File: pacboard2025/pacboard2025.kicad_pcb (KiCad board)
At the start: 4 copper layers, 28 parts, among them J1 XT30 Male Connector, U2 D24V50F5, U3 ProS3, U6 BNO085

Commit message: some changes to pcb
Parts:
- Conn_01x04_Socket1: footprint board1_footprints:Stemma QT -> Connector_JST:JST_SH_SM04B-SRSS-TB_1x04-1MP_P1.00mm_Horizontal
- moved Conn_01x04_Socket1 51.5 mm to (167.6, 93.3), turned to 90 degrees
- moved MOTOR2 25.4 mm to (165.4, 132.8)
- moved MC2 12.6 mm to (150.4, 141.9)
- moved XSHUT_CONN1 12.4 mm to (114.6, 132.6)
- moved C1 12.4 mm to (109.8, 113.4)
- moved C2 12.4 mm to (104.1, 113.4)
- moved C3 12.4 mm to (98.2, 113.4)
- moved LED1 12.4 mm to (110.0, 108.8)
- moved LED3 12.4 mm to (98.2, 108.7)
- moved R2 12.4 mm to (114.4, 108.6)
- moved U6 12.4 mm to (99.0, 115.9)
- moved C4 12.4 mm to (92.1, 113.5)
- moved LED2 12.4 mm to (104.1, 108.8)
- moved LED4 12.4 mm to (92.2, 108.7)
- moved J1 10.4 mm to (152.3, 112.5)
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
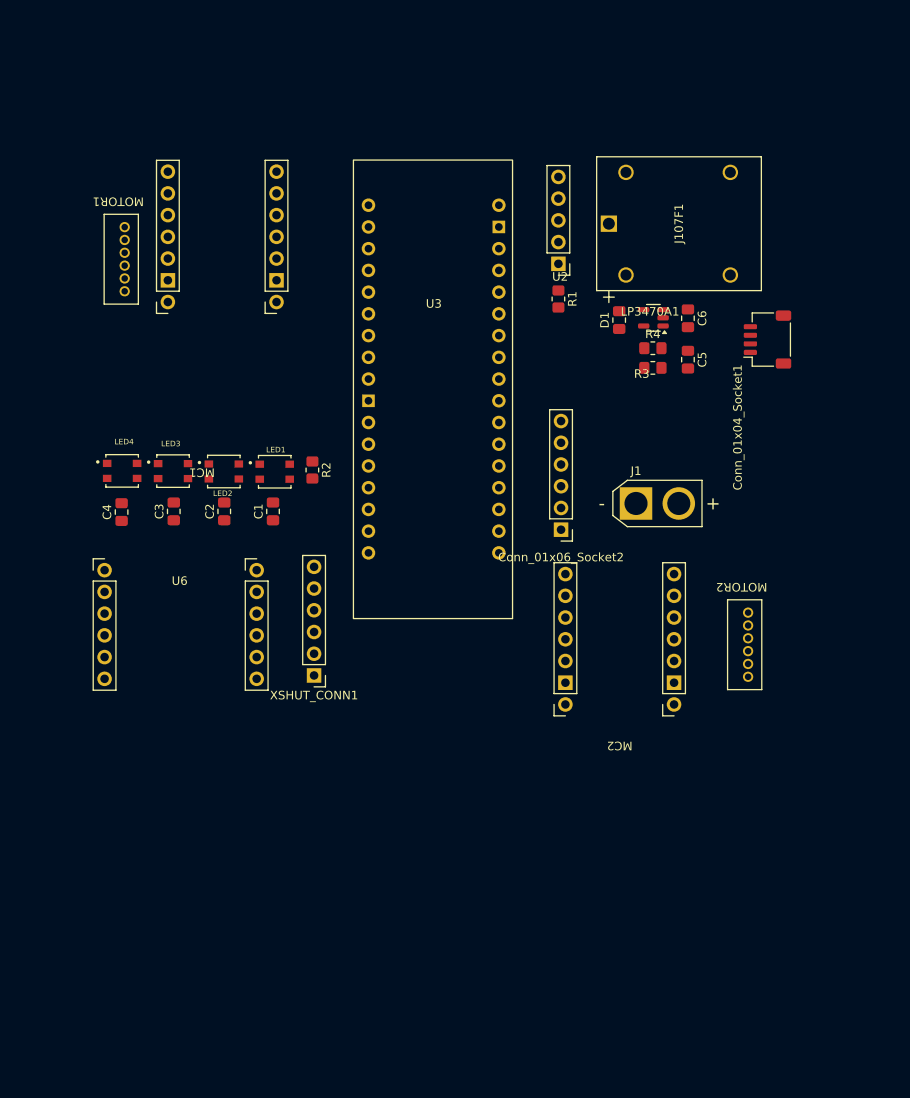
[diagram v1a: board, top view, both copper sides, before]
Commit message: Changed layout to account for battery and motors, tried routing stuff
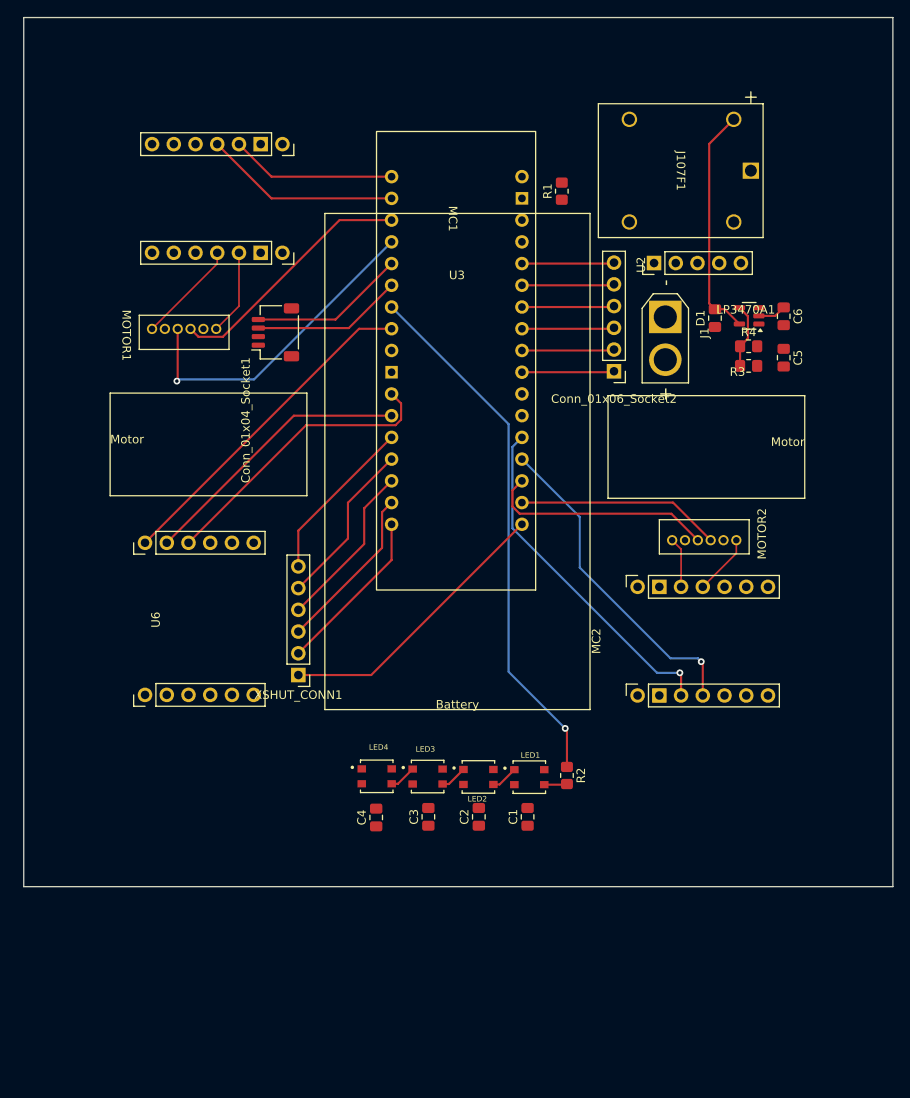
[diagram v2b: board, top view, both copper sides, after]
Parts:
- moved Conn_01x04_Socket1 57.5 mm to (110.1, 92.5)
- moved C4 46.5 mm to (121.9, 149.2)
- moved LED4 46.5 mm to (122.0, 144.4)
- moved LED1 46.5 mm to (139.8, 144.5)
- moved LED3 46.5 mm to (127.9, 144.4)
- moved R2 46.5 mm to (144.2, 144.3)
- moved C2 46.5 mm to (133.9, 149.1)
- moved C3 46.5 mm to (128.0, 149.1)
- moved LED2 46.5 mm to (133.8, 144.5)
- moved C1 46.5 mm to (139.6, 149.1)
- moved MC1 22.1 mm to (116.8, 76.8), turned to -90 degrees
- moved J1 22.1 mm to (155.7, 90.7), turned to -90 degrees
- moved Conn_01x06_Socket2 19.5 mm to (149.7, 97.0)
- moved MOTOR2 18.3 mm to (156.5, 116.8), turned to 90 degrees
- moved J107F1 17.7 mm to (165.7, 73.6), turned to -90 degrees
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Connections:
- U3 pad 13: /1_ENCA -> /2_PWM1
- U3 pad 14: /1_ENCB -> /2_PWM2
- U3 pad 31: /2_PWM2 -> /1_ENCB
- U3 pad 32: /2_PWM1 -> /1_ENCA
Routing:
- net /+12V: track 0.00 -> 132.6 mm
- net /5V: track 0.00 -> 129.8 mm
- net /BAT_12V: track 0.00 -> 63.1 mm
- net /LED_DATA: track 0.00 -> 62.3 mm, vias 0 -> 1
- net /2_PWM1: track 0.00 -> 40.4 mm, vias 0 -> 1
- net /IMU_INTR: track 0.00 -> 39.2 mm
- net /2_PWM2: track 0.00 -> 38.3 mm, vias 0 -> 1
- net /1_ENCB: track 0.00 -> 38.0 mm, vias 0 -> 1
- net /UART_TX: track 0.00 -> 34.3 mm
- net /XSHUT_TOF6: track 0.00 -> 33.4 mm
- net /UART_RX: track 0.00 -> 32.4 mm
- net /1_ENCA: track 0.00 -> 29.5 mm
- net Net-(D1-A): track 0.00 -> 27.2 mm
- net /2_ENCA: track 0.00 -> 26.8 mm
- net /2_ENCB: track 0.00 -> 23.9 mm
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- added copper zone on In2.Cu, net /+3.3V
- added copper zone on In1.Cu, net /GND
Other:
- board outline added: 101.6 x 101.6 mm
- board text added: "Battery"
- board text added: "Motor"

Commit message: new chassis shape
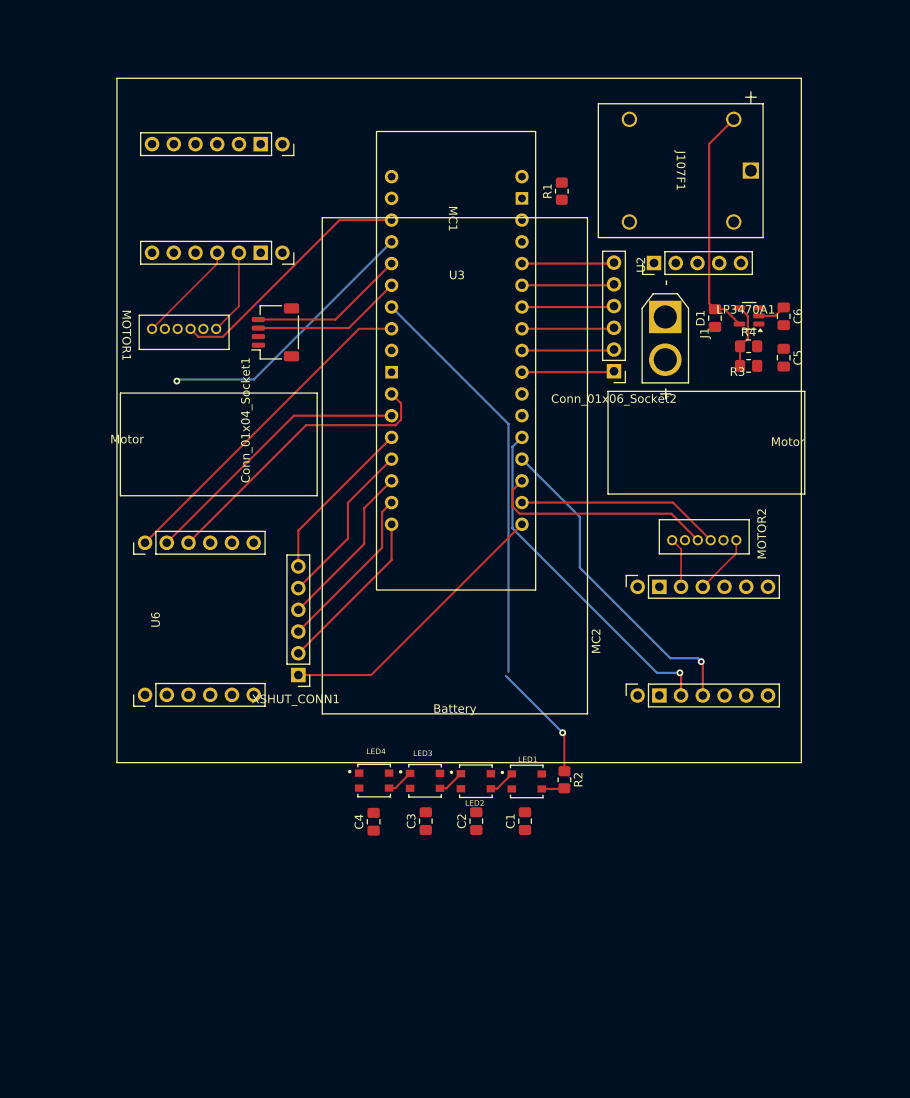
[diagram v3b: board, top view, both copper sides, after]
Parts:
- moved C2 0.58 mm to (133.6, 149.6)
- moved C4 0.58 mm to (121.6, 149.7)
- moved LED1 0.58 mm to (139.5, 145.0)
- moved LED4 0.58 mm to (121.7, 144.9)
- moved C3 0.58 mm to (127.7, 149.6)
- moved LED3 0.58 mm to (127.6, 144.9)
- moved C1 0.58 mm to (139.3, 149.6)
- moved LED2 0.58 mm to (133.6, 145.0)
- moved R2 0.58 mm to (143.9, 144.8)
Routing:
- net /+12V: track 132.6 -> 98.1 mm
- net /1_PWM2: track 23.0 -> 0.00 mm
- net /1_PWM1: track 19.4 -> 0.00 mm
- net /1_ENCB: track 38.0 -> 32.0 mm
- removed copper zone on In2.Cu, net /+3.3V
- removed copper zone on In1.Cu, net /GND
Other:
- board outline removed

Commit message: changed PCB dimensions
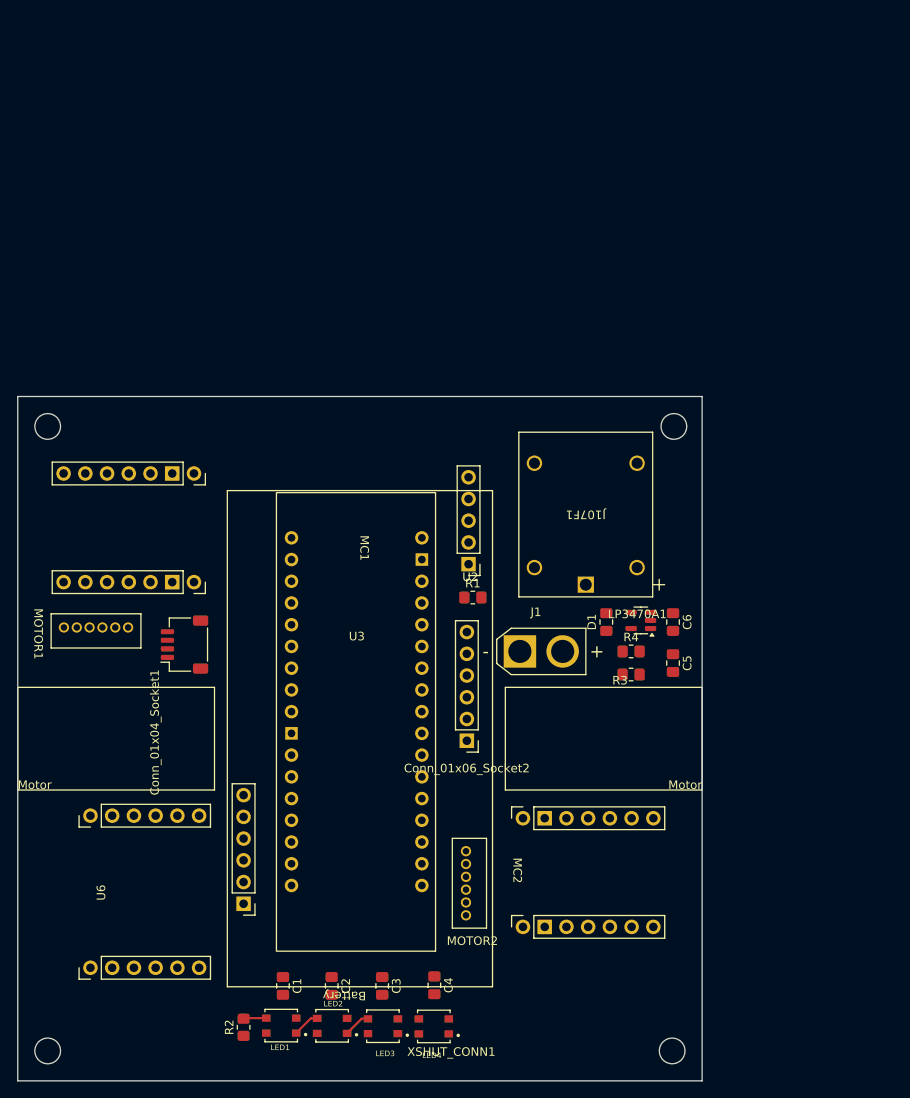
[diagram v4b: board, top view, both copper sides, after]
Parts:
- moved J107F1 52.1 mm to (146.4, 122.0), turned to 180 degrees
- moved R1 48.6 mm to (133.2, 123.5), turned to 0 degrees
- moved R2 47.4 mm to (106.4, 173.7), turned to 90 degrees
- moved Conn_01x06_Socket2 46.5 mm to (132.5, 140.2)
- moved U3 43.8 mm to (119.6, 136.8)
- moved MOTOR2 43.6 mm to (132.4, 153.2), turned to 0 degrees
- moved J1 42.6 mm to (138.7, 129.8), turned to 0 degrees
- moved U2 41.3 mm to (132.7, 119.6), turned to 180 degrees
- moved LED1 40.5 mm to (110.8, 173.5), turned to 180 degrees
- moved MC1 39.9 mm to (106.5, 115.3)
- moved R3 38.6 mm to (151.7, 132.5)
- moved R4 38.2 mm to (151.7, 129.8)
- moved Conn_01x04_Socket1 38.0 mm to (99.5, 129.0)
- moved C6 38.0 mm to (156.6, 126.4)
- moved C5 38.0 mm to (156.6, 131.2)
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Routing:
- net /+12V: track 98.1 -> 0.00 mm
- net /5V: track 129.8 -> 43.0 mm
- net /BAT_12V: track 63.1 -> 0.00 mm
- net /LED_DATA: track 62.3 -> 0.00 mm, vias 1 -> 0
- net /2_PWM1: track 40.4 -> 0.00 mm, vias 1 -> 0
- net /IMU_INTR: track 39.2 -> 0.00 mm
- net /2_PWM2: track 38.3 -> 0.00 mm, vias 1 -> 0
- net /UART_TX: track 34.3 -> 0.00 mm
- net /XSHUT_TOF6: track 33.4 -> 0.00 mm
- net /UART_RX: track 32.4 -> 0.00 mm
- net /1_ENCB: track 32.0 -> 0.00 mm, vias 1 -> 0
- net /1_ENCA: track 29.5 -> 0.00 mm
- net Net-(D1-A): track 27.2 -> 0.00 mm
- net /2_ENCA: track 26.8 -> 0.00 mm
- net /2_ENCB: track 23.9 -> 0.00 mm
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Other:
- board outline added: 80 x 80 mm
